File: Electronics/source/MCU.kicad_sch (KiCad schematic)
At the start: 51 parts, among them J1 Conn_01x05, J16 Conn_01x02, J2 Conn_01x03, J22 Conn_01x04, J3 Conn_01x03, J4 Conn_01x05, J6 Conn_01x20, J7 Conn_01x20, SW10 SW_Push, SW11 SW_Push, SW12 SW_Push, SW13 SW_Push, SW14 SW_Coded, SW4 SW_Push, SW5 SW_SPDT, SW6 SW_SPDT, SW7 SW_SPDT, SW8 SW_Push, SW9 SW_Push, U1 STM32F072CBTx, U5 ADP122AUJZ-3.3-R7, Y1 ABL-8.000MHZ-B2

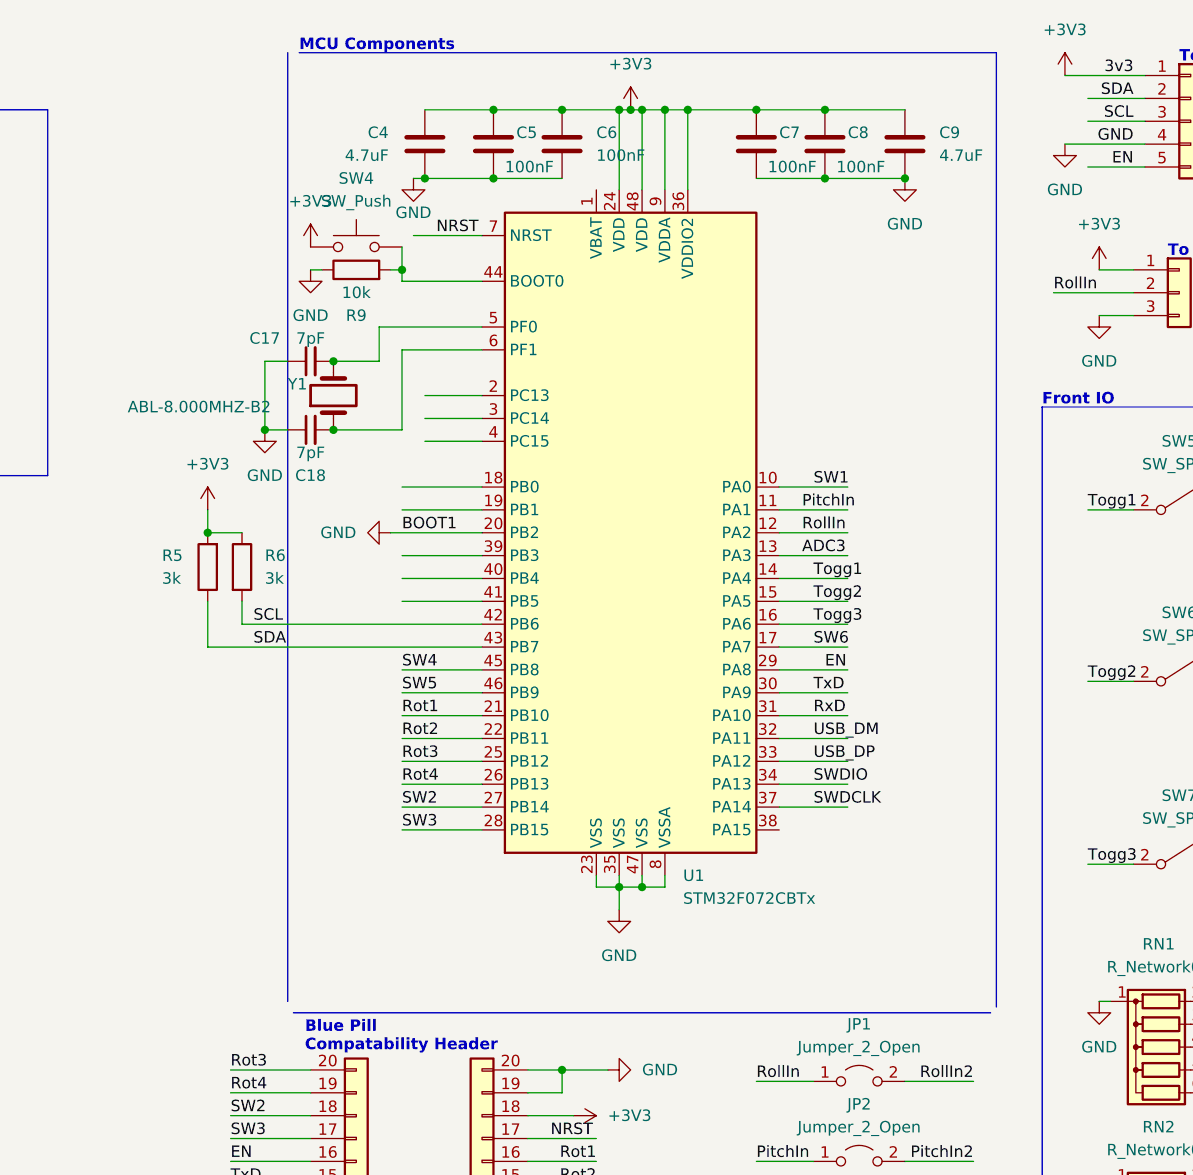
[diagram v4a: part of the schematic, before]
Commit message: small bug fixes and clock stability
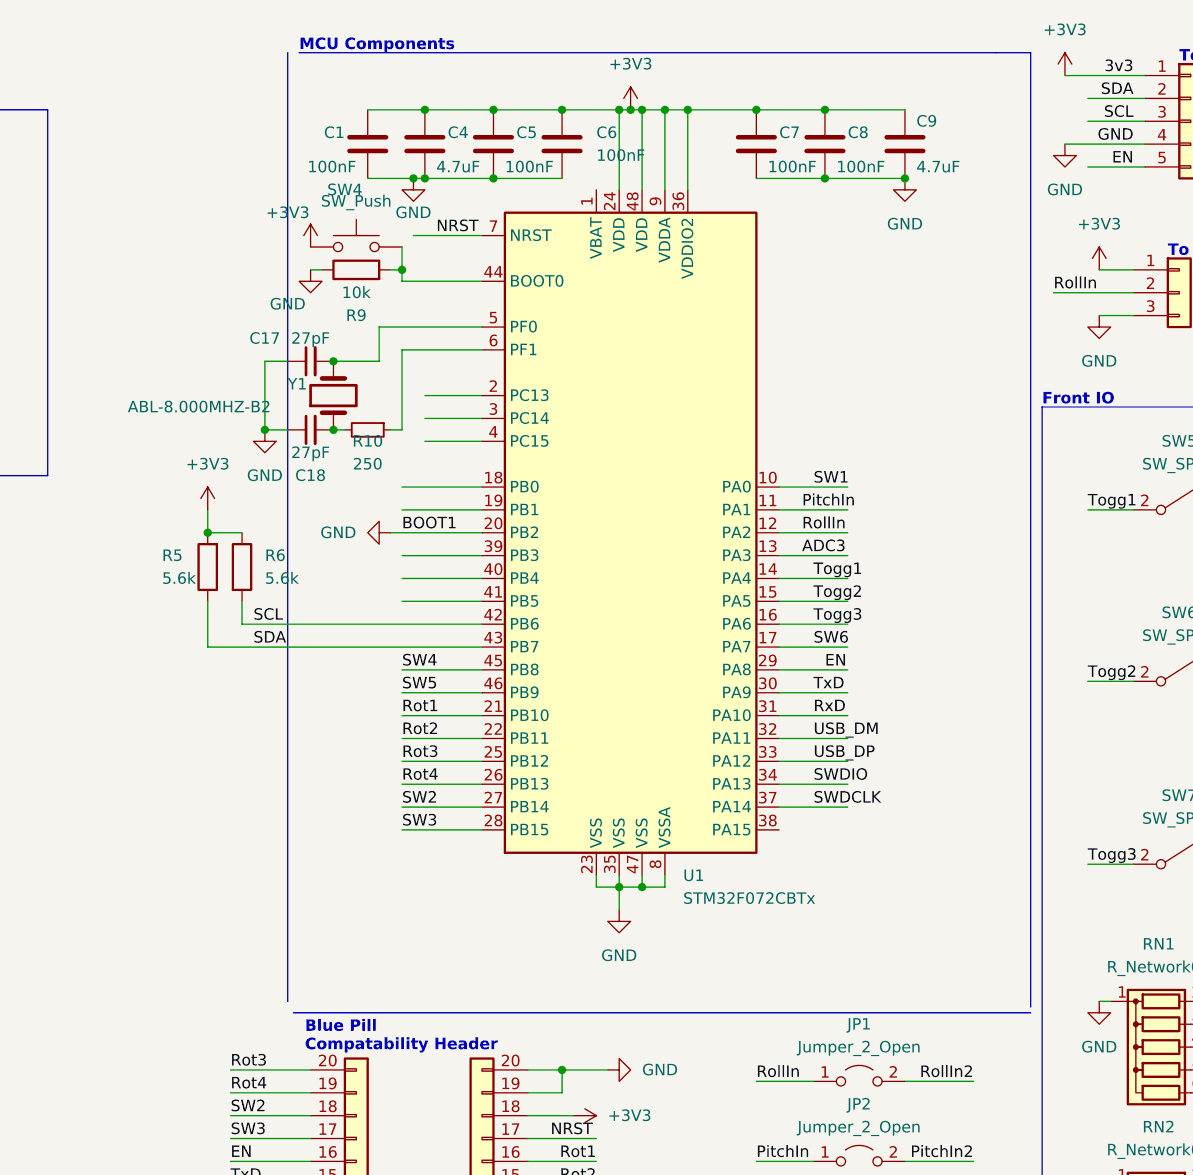
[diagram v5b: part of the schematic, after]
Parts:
- added C1: 100nF, Capacitor_SMD:C_0805_2012Metric, symbol Device:C
- added R10: 250, Resistor_SMD:R_0603_1608Metric, symbol Device:R_Small
- C17, C18: value 7pF -> 27pF
- R5, R6: value 3k -> 5.6k
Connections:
- net +3V3: now also C1.1
- net GND: now also C1.2
- net at C18.2, Y1.1: now also R10.2; no longer U1.6 (PF1)
- new net: R10.1, U1.6 (PF1)
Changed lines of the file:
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@@
   (junction (at 124.46 31.75) (diameter 0) (color 0 0 0 0)
   )
+  (junction (at 168.91 24.13) (diameter 0) (color 0 0 0 0)
+  )
+  (junction (at 44.45 181.61) (diameter 0) (color 0 0 0 0)
+  )
+  (junction (at 151.13 24.13) (diameter 0) (color 0 0 0 0)
+  )
+  (junction (at 123.19 31.75) (diameter 0) (color 0 0 0 0)
+  )
+  (junction (at 247.65 121.92) (diameter 0) (color 0 0 0 0)
+  )
   (junction (at 114.3 59.69) (diameter 0) (color 0 0 0 0)
   )
-  (junction (at 168.91 24.13) (diameter 0) (color 0 0 0 0)
-  )
-  (junction (at 44.45 181.61) (diameter 0) (color 0 0 0 0)
-  )
-  (junction (at 151.13 24.13) (diameter 0) (color 0 0 0 0)
-  )
-  (junction (at 247.65 121.92) (diameter 0) (color 0 0 0 0)
-  )
   (junction (at 148.59 24.13) (diameter 0) (color 0 0 0 0)
   )
@@
   )
   (junction (at 146.05 24.13) (diameter 0) (color 0 0 0 0)
+  )
+  (junction (at 124.46 24.13) (diameter 0) (color 0 0 0 0)
   )
   (junction (at 139.7 24.13) (diameter 0) (color 0 0 0 0)
@@
     (stroke (width 0) (type default) (color 0 0 0 0))
   )
+  (polyline (pts (xy 187.96 17.78) (xy 191.77 17.78))
+    (stroke (width 0) (type default) (color 0 0 0 0))
+  )
   (wire (pts (xy 210.82 125.73) (xy 214.63 125.73))
     (stroke (width 0) (type default) (color 0 0 0 0))
   )
+  (wire (pts (xy 120.65 59.69) (xy 121.92 59.69))
+    (stroke (width 0) (type default) (color 0 0 0 0))
+  )
   (wire (pts (xy 135.89 166.37) (xy 143.51 166.37))
     (stroke (width 0) (type default) (color 0 0 0 0))
@@
     (stroke (width 0) (type default) (color 0 0 0 0))
   )
+  (wire (pts (xy 114.3 59.69) (xy 115.57 59.69))
+    (stroke (width 0) (type default) (color 0 0 0 0))
+  )
   (wire (pts (xy 67.31 35.56) (xy 67.31 41.91))
     (stroke (width 0) (type default) (color 0 0 0 0))
@@
     (stroke (width 0) (type default) (color 0 0 0 0))
   )
-  (polyline (pts (xy 187.325 124.46) (xy 109.855 124.46))
+  (polyline (pts (xy 191.77 124.46) (xy 109.855 124.46))
     (stroke (width 0) (type default) (color 0 0 0 0))
   )
@@
     (stroke (width 0) (type default) (color 0 0 0 0))
   )
-  (polyline (pts (xy 187.96 17.78) (xy 187.96 123.825))
+  (polyline (pts (xy 191.77 17.78) (xy 191.77 123.825))
     (stroke (width 0) (type default) (color 0 0 0 0))
   )
@@
     (stroke (width 0) (type default) (color 0 0 0 0))
   )
-  (wire (pts (xy 114.3 59.69) (xy 121.92 59.69))
-    (stroke (width 0) (type default) (color 0 0 0 0))
-  )
   (wire (pts (xy 213.36 71.12) (xy 214.63 71.12))
     (stroke (width 0) (type default) (color 0 0 0 0))
@@
     (stroke (width 0) (type default) (color 0 0 0 0))
   )
+  (wire (pts (xy 118.11 31.75) (xy 123.19 31.75))
+    (stroke (width 0) (type default) (color 0 0 0 0))
+  )
   (wire (pts (xy 135.89 163.83) (xy 143.51 163.83))
     (stroke (width 0) (type default) (color 0 0 0 0))
@@
   )
   (wire (pts (xy 274.32 154.94) (xy 276.86 154.94))
+    (stroke (width 0) (type default) (color 0 0 0 0))
+  )
+  (wire (pts (xy 118.11 24.13) (xy 124.46 24.13))
     (stroke (width 0) (type default) (color 0 0 0 0))
   )
@@
       (effects (font (size 1.27 1.27)) (justify left))
     )
-    (property "Value" "3k" (id 1) (at 106.68 76.1999 0)
+    (property "Value" "5.6k" (id 1) (at 106.68 76.1999 0)
       (effects (font (size 1.27 1.27)) (justify left))
     )
@@
     (in_bom yes) (on_board yes)
     (property "Reference" "C17" (id 0) (at 106.68 49.53 90))
-    (property "Value" "7pF" (id 1) (at 111.76 49.53 90))
+    (property "Value" "27pF" (id 1) (at 111.76 49.53 90))
     (property "Footprint" "Capacitor_SMD:C_0603_1608Metric" (id 2) (at 111.76 52.07 0)
       (effects (font (size 1.27 1.27)) hide)
@@
     (pin "5")
   )
+  (symbol (lib_id "Device:R_Small") (at 118.11 59.69 270) (unit 1)
+    (in_bom yes) (on_board yes)
+    (property "Reference" "R10" (id 0) (at 118.11 60.96 90))
+    (property "Value" "250" (id 1) (at 118.11 63.5 90))
+    (property "Footprint" "Resistor_SMD:R_0603_1608Metric" (id 2) (at 118.11 59.69 0)
+      (effects (font (size 1.27 1.27)) hide)
+    )
+    (property "Datasheet" "~" (id 3) (at 118.11 59.69 0)
+      (effects (font (size 1.27 1.27)) hide)
+    )
+    (pin "1")
+    (pin "2")
+  )
   (symbol (lib_id "power:+3V3") (at 236.22 41.91 0) (unit 1)
     (in_bom yes) (on_board yes) (fields_autoplaced)
@@
   (symbol (lib_id "Device:C") (at 124.46 27.94 0) (unit 1)
     (in_bom yes) (on_board yes)
-    (property "Reference" "C4" (id 0) (at 118.11 26.67 0)
-      (effects (font (size 1.27 1.27)) (justify left))
-    )
-    (property "Value" "4.7uF" (id 1) (at 115.57 29.21 0)
+    (property "Reference" "C4" (id 0) (at 127 26.67 0)
+      (effects (font (size 1.27 1.27)) (justify left))
+    )
+    (property "Value" "4.7uF" (id 1) (at 125.73 30.48 0)
       (effects (font (size 1.27 1.27)) (justify left))
     )
@@
   )
   (symbol (lib_id "Device:C") (at 177.8 27.94 0) (unit 1)
-    (in_bom yes) (on_board yes) (fields_autoplaced)
-    (property "Reference" "C9" (id 0) (at 181.61 26.6699 0)
-      (effects (font (size 1.27 1.27)) (justify left))
-    )
-    (property "Value" "4.7uF" (id 1) (at 181.61 29.2099 0)
+    (in_bom yes) (on_board yes)
+    (property "Reference" "C9" (id 0) (at 179.07 25.4 0)
+      (effects (font (size 1.27 1.27)) (justify left))
+    )
+    (property "Value" "4.7uF" (id 1) (at 179.07 30.48 0)
       (effects (font (size 1.27 1.27)) (justify left))
     )
@@
       (effects (font (size 1.27 1.27)) (justify right))
     )
-    (property "Value" "3k" (id 1) (at 95.25 76.2 0)
+    (property "Value" "5.6k" (id 1) (at 95.25 76.2 0)
       (effects (font (size 1.27 1.27)) (justify right))
     )
@@
     (pin "3")
   )
+  (symbol (lib_id "Device:C") (at 118.11 27.94 0) (mirror y) (unit 1)
+    (in_bom yes) (on_board yes)
+    (property "Reference" "C1" (id 0) (at 115.57 26.67 0)
+      (effects (font (size 1.27 1.27)) (justify left))
+    )
+    (property "Value" "100nF" (id 1) (at 116.84 30.48 0)
+      (effects (font (size 1.27 1.27)) (justify left))
+    )
+    (property "Footprint" "Capacitor_SMD:C_0805_2012Metric" (id 2) (at 117.1448 31.75 0)
+      (effects (font (size 1.27 1.27)) hide)
+    )
+    (property "Datasheet" "~" (id 3) (at 118.11 27.94 0)
+      (effects (font (size 1.27 1.27)) hide)
+    )
+    (pin "1")
+    (pin "2")
+  )
   (symbol (lib_id "Switch:SW_Push") (at 269.24 121.92 0) (unit 1)
     (in_bom yes) (on_board yes) (fields_autoplaced)
@@
   )
   (symbol (lib_id "power:+3V3") (at 111.76 39.37 0) (unit 1)
-    (in_bom yes) (on_board yes) (fields_autoplaced)
+    (in_bom yes) (on_board yes)
     (property "Reference" "#PWR0164" (id 0) (at 111.76 43.18 0)
       (effects (font (size 1.27 1.27)) hide)
     )
-    (property "Value" "+3V3" (id 1) (at 111.76 34.29 0))
+    (property "Value" "+3V3" (id 1) (at 109.22 35.56 0))
     (property "Footprint" "" (id 2) (at 111.76 39.37 0)
       (effects (font (size 1.27 1.27)) hide)
@@
     (in_bom yes) (on_board yes)
     (property "Reference" "C18" (id 0) (at 111.76 64.77 90))
-    (property "Value" "7pF" (id 1) (at 111.76 62.23 90))
+    (property "Value" "27pF" (id 1) (at 111.76 62.23 90))
     (property "Footprint" "Capacitor_SMD:C_0603_1608Metric" (id 2) (at 111.76 59.69 0)
       (effects (font (size 1.27 1.27)) hide)
@@
   )
   (symbol (lib_id "power:GND") (at 111.76 41.91 0) (unit 1)
-    (in_bom yes) (on_board yes) (fields_autoplaced)
+    (in_bom yes) (on_board yes)
     (property "Reference" "#PWR0163" (id 0) (at 111.76 48.26 0)
       (effects (font (size 1.27 1.27)) hide)
     )
-    (property "Value" "GND" (id 1) (at 111.76 46.99 0))
+    (property "Value" "GND" (id 1) (at 109.22 45.72 0))
     (property "Footprint" "" (id 2) (at 111.76 41.91 0)
       (effects (font (size 1.27 1.27)) hide)
@@
   )
   (symbol (lib_id "Switch:SW_Push") (at 116.84 39.37 0) (unit 1)
-    (in_bom yes) (on_board yes) (fields_autoplaced)
-    (property "Reference" "SW4" (id 0) (at 116.84 31.75 0))
+    (in_bom yes) (on_board yes)
+    (property "Reference" "SW4" (id 0) (at 115.57 33.02 0))
     (property "Value" "SW_Push" (id 1) (at 116.84 34.29 0))
     (property "Footprint" "Button_Switch_THT:SW_PUSH_6mm" (id 2) (at 116.84 34.29 0)
@@
   (symbol (lib_id "power:+3V3") (at 43.18 91.44 0) (unit 1)
     (in_bom yes) (on_board yes) (fields_autoplaced)
-    (property "Reference" "#PWR?" (id 0) (at 43.18 95.25 0)
-      (effects (font (size 1.27 1.27)) hide)
-    )
+    (property "Reference" "#PWR0134" (id 0) (at 43.18 95.25 0)
+      (effects (font (size 1.27 1.27)) hide)
+    )

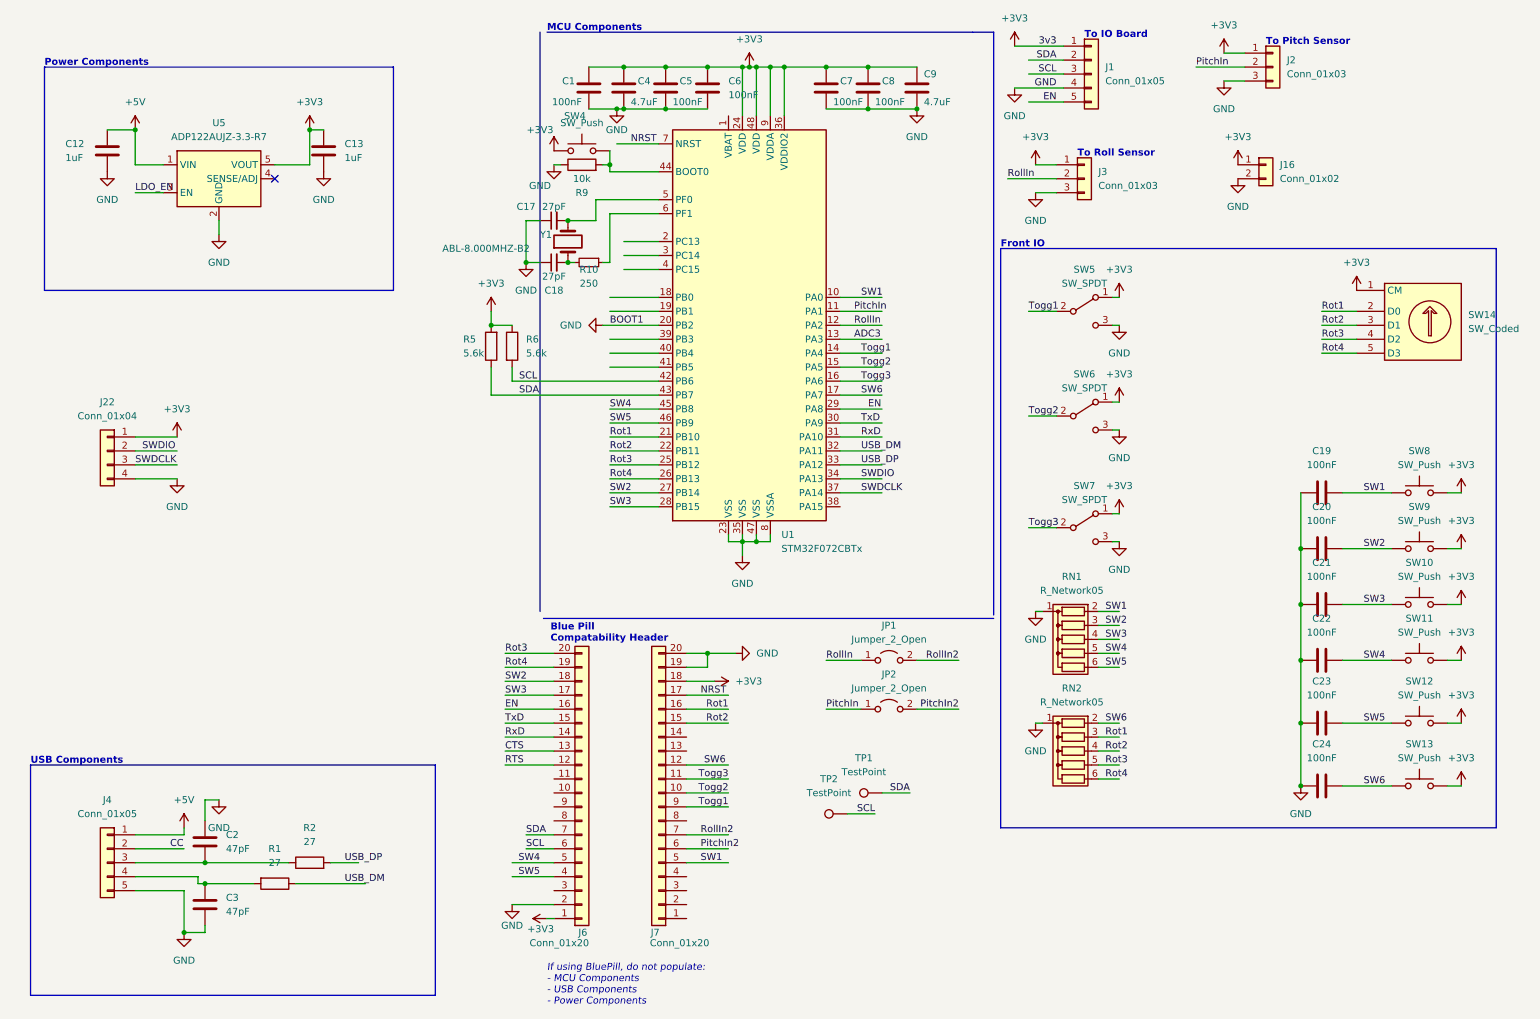
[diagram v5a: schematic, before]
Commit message: added firmware submodule to firmware repo
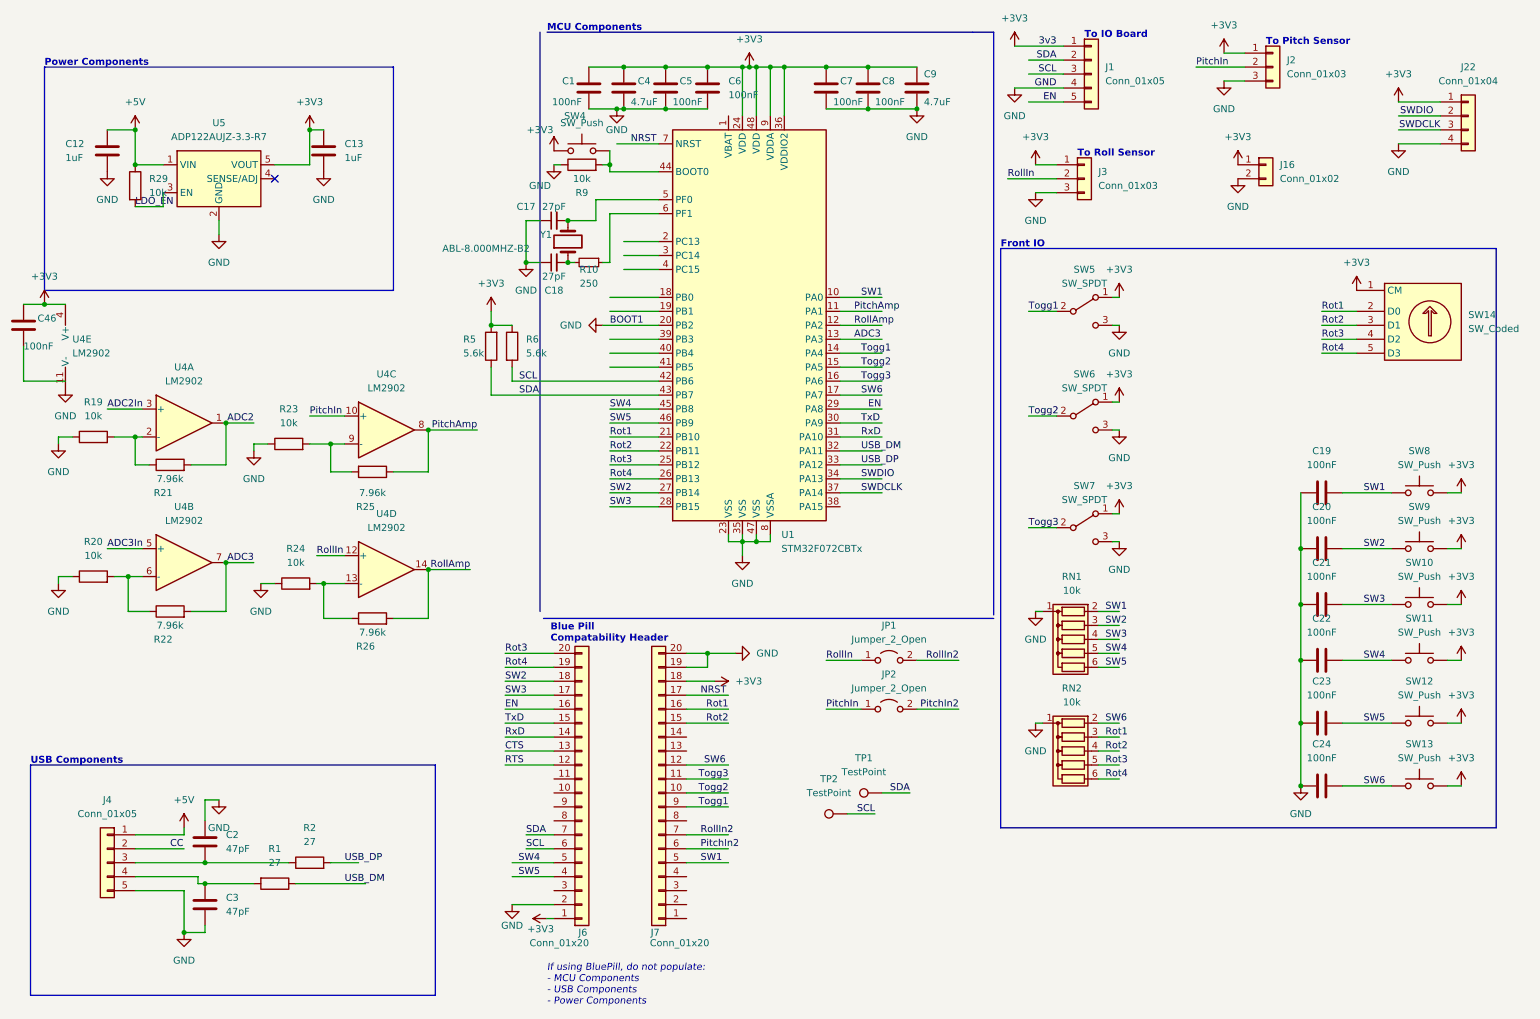
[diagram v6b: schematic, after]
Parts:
- added C46: 100nF, Capacitor_SMD:C_0603_1608Metric, symbol Device:C
- added R19, R20, R23, R24: 10k, Resistor_SMD:R_0603_1608Metric, symbol Device:R
- added R21, R22, R25, R26: 7.96k, Resistor_SMD:R_0603_1608Metric, symbol Device:R
- added R29: 10k, Capacitor_SMD:C_0805_2012Metric, symbol Device:R
- added U4: LM2902, Package_SO:TSSOP-14_4.4x5mm_P0.65mm, symbol Amplifier_Operational:LM2902
- RN1, RN2: value R_Network05 -> 10k
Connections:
- net +3V3: now also C46.1, U4.4 (V+)
- net +5V: now also R29.1
- net ADC3: now also R22.2, U4.7
- net GND: now also R19.1, R20.1, R23.1, R24.1, U4.11 (V-)
- net LDO_EN: now also R29.2
- net PitchIn: now also U4.10 (+); no longer U1.11 (PA1)
- net RollIn: now also U4.12 (+); no longer U1.12 (PA2)
- new net: R19.2, R21.1, U4.2 (-)
- new net: R23.2, R25.2, U4.9 (-)
- new net: R20.2, R22.1, U4.6 (-)
- new net: R24.2, R26.1, U4.13 (-)
- new net ADC2: R21.2, U4.1
- new net ADC2In: U4.3 (+)
- new net ADC3In: U4.5 (+)
- new net PitchAmp: R25.1, U1.11 (PA1), U4.8
- new net RollAmp: R26.2, U1.12 (PA2), U4.14
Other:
- moved on the sheet: J22
